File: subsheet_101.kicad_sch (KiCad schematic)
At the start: 6 parts, among them J03 Jumper wire, J04 Jumper wire

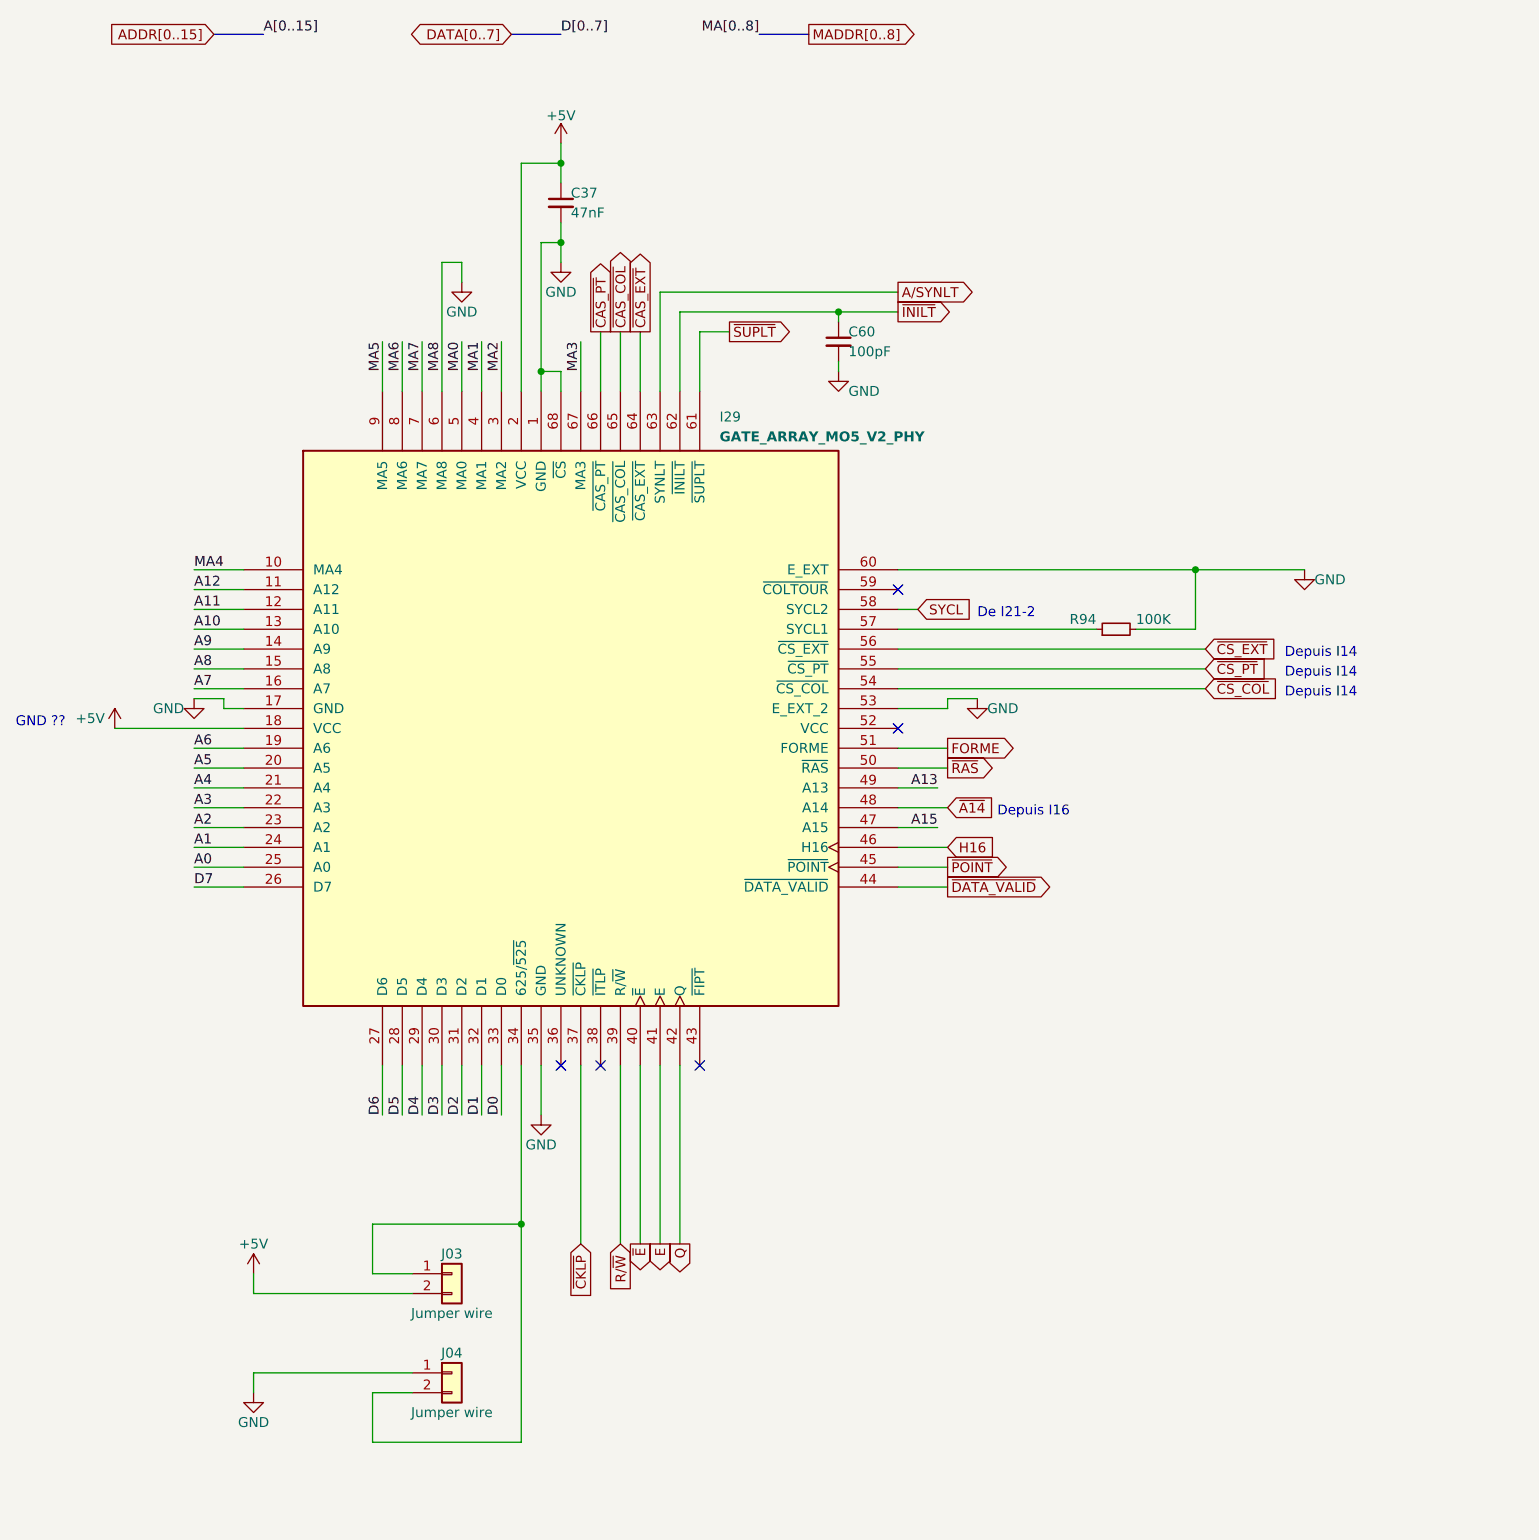
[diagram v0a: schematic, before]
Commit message: Various mentions, added C60bis to I29 on pin 62
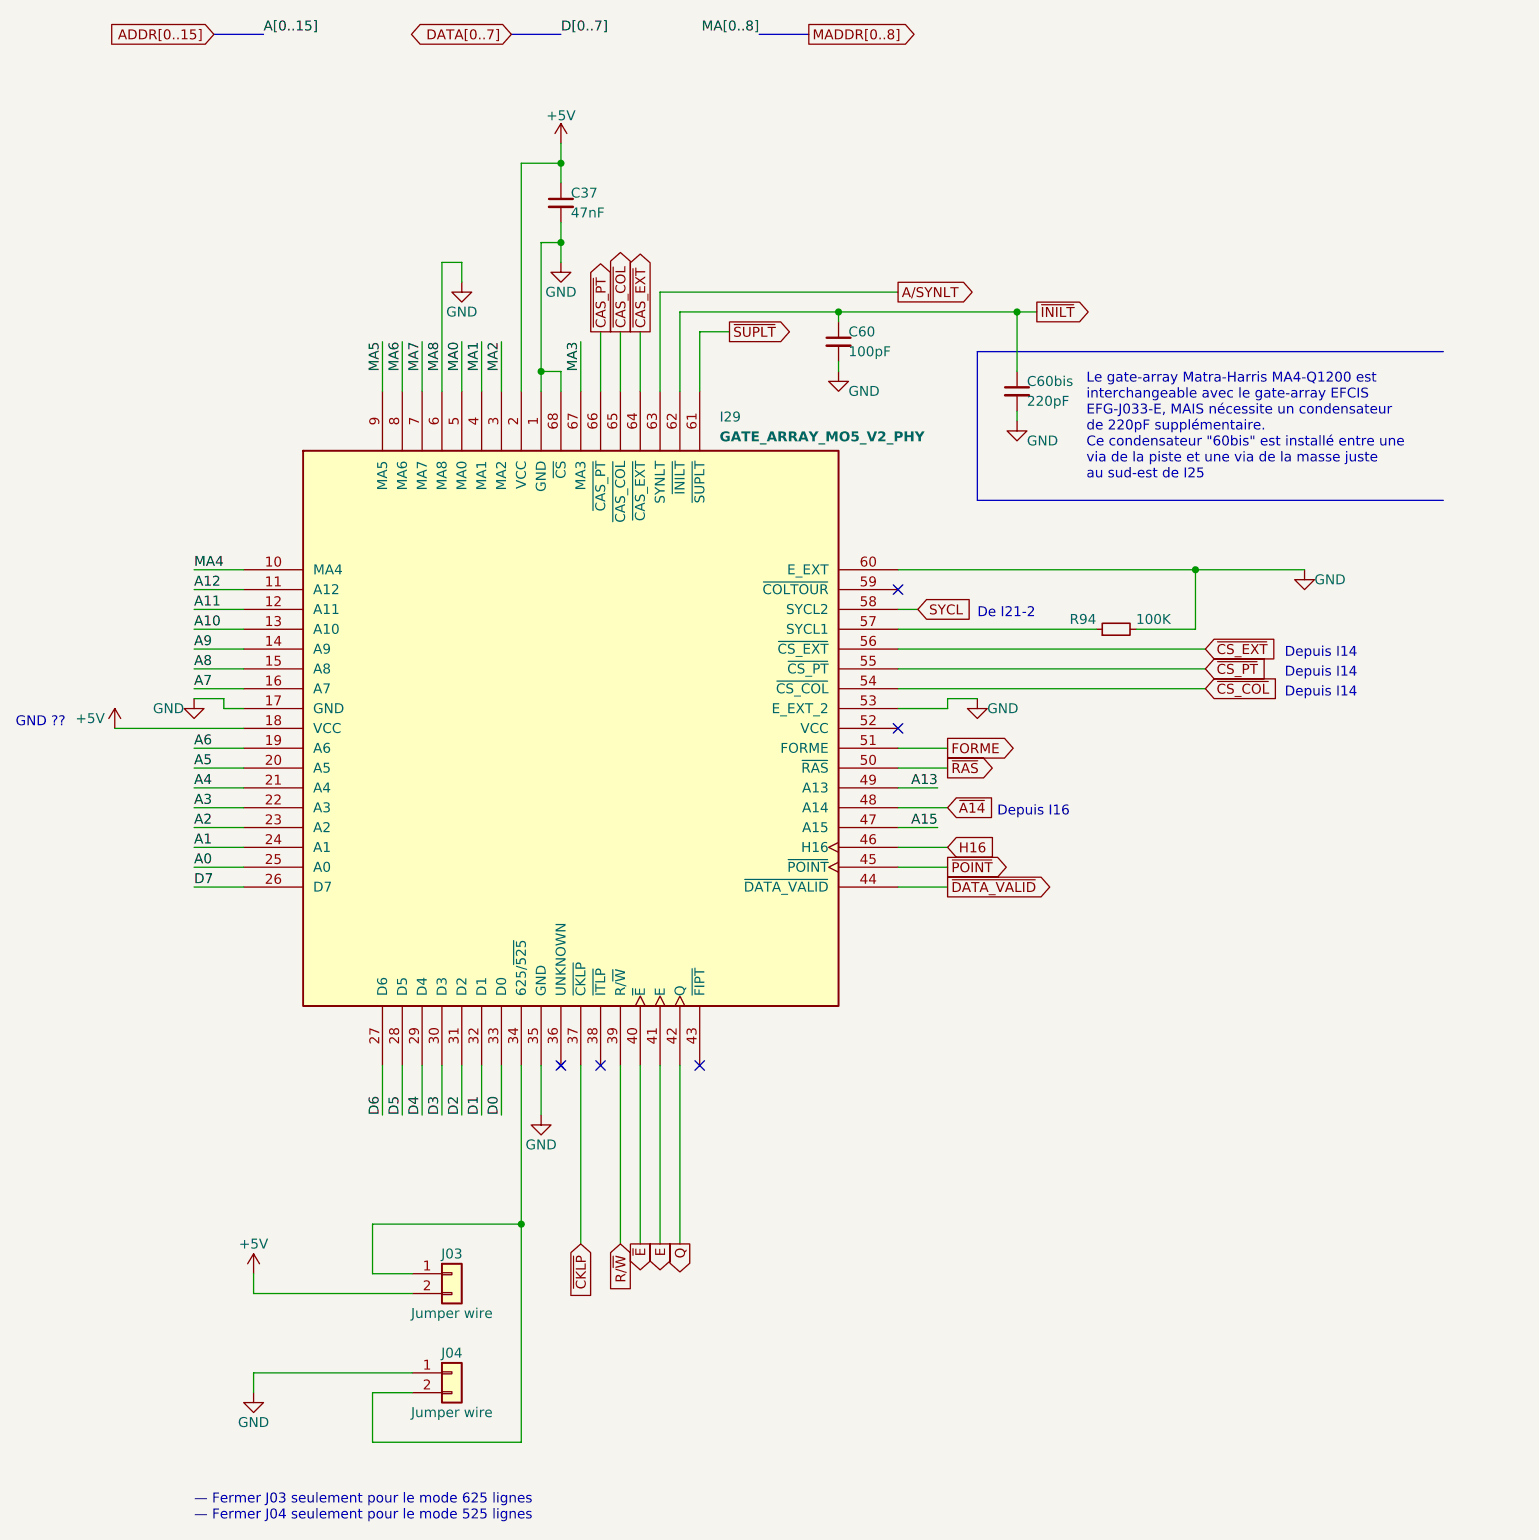
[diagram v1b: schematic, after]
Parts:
- added C60bis: 220pF, commons-passives_THT:Passive_THT_capacitor_mlcc_W2.54mm_L5.08mm, symbol Device:C_Small
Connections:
- net GND: now also C60bis.2
- net ~{INILT}: now also C60bis.1
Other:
- note added: "Le gate-array Matra-Harris MA4-Q1200 est interchangeable avec le gate-array EFCIS EFG-J033-E, MAIS nécessite un condensateur de 220pF supplémentaire. Ce condensateur "60bis" est installé entre une via de la piste et une via de la masse juste au sud-est de I25"
- note added: "— Fermer J03 seulement pour le mode 625 lignes — Fermer J04 seulement pour le mode 525 lignes"
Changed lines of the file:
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@@
   (junction (at 118.11 60.96) (diameter 0) (color 0 0 0 0)
+  )
+  (junction (at 140.97 60.96) (diameter 0) (color 0 0 0 0)
   )
   (junction (at 80.01 68.58) (diameter 0) (color 0 0 0 0)
@@
     (stroke (width 0) (type default))
   )
+  (wire (pts (xy 140.97 73.66) (xy 140.97 74.93))
+    (stroke (width 0) (type default))
+  )
   (wire (pts (xy 156.21 101.6) (xy 163.83 101.6))
     (stroke (width 0) (type default))
@@
     (stroke (width 0) (type default))
   )
-  (wire (pts (xy 125.73 60.96) (xy 118.11 60.96))
-    (stroke (width 0) (type default))
-  )
   (wire (pts (xy 59.69 64.77) (xy 59.69 71.12))
     (stroke (width 0) (type default))
@@
     (stroke (width 0) (type default))
   )
+  (polyline (pts (xy 135.89 85.09) (xy 195.58 85.09))
+    (stroke (width 0) (type default))
+  )
   (wire (pts (xy 118.11 67.31) (xy 118.11 68.58))
     (stroke (width 0) (type default))
@@
     (stroke (width 0) (type default))
   )
+  (wire (pts (xy 143.51 60.96) (xy 140.97 60.96))
+    (stroke (width 0) (type default))
+  )
   (wire (pts (xy 67.31 163.83) (xy 67.31 157.48))
     (stroke (width 0) (type default))
@@
     (stroke (width 0) (type default))
   )
+  (polyline (pts (xy 195.58 66.04) (xy 135.89 66.04))
+    (stroke (width 0) (type default))
+  )
   (wire (pts (xy 85.09 157.48) (xy 85.09 180.34))
     (stroke (width 0) (type default))
@@
     (stroke (width 0) (type default))
   )
+  (wire (pts (xy 140.97 60.96) (xy 140.97 68.58))
+    (stroke (width 0) (type default))
+  )
+  (polyline (pts (xy 135.89 66.04) (xy 135.89 85.09))
+    (stroke (width 0) (type default))
+  )
   (wire (pts (xy 77.47 41.91) (xy 82.55 41.91))
     (stroke (width 0) (type default))
@@
     (stroke (width 0) (type default))
   )
+  (wire (pts (xy 118.11 60.96) (xy 140.97 60.96))
+    (stroke (width 0) (type default))
+  )
   (wire (pts (xy 35.56 127) (xy 41.91 127))
     (stroke (width 0) (type default))
@@
     (effects (font (size 1.27 1.27)) (justify left bottom))
   )
+  (text "— Fermer J03 seulement pour le mode 625 lignes\n— Fermer J04 seulement pour le mode 525 lignes"
+    (at 35.56 215.9 0)
+    (effects (font (size 1.27 1.27)) (justify left bottom))
+  )
   (text "Depuis I14" (at 175.26 105.41 0)
+    (effects (font (size 1.27 1.27)) (justify left bottom))
+  )
+  (text "Le gate-array Matra-Harris MA4-Q1200 est\ninterchangeable avec le gate-array EFCIS\nEFG-J033-E, MAIS nécessite un condensateur\nde 220pF supplémentaire.\nCe condensateur \"60bis\" est installé entre une\nvia de la piste et une via de la masse juste\nau sud-est de I25"
+    (at 149.86 82.55 0)
     (effects (font (size 1.27 1.27)) (justify left bottom))
   )
@@
     )
   )
-  (global_label "~{INILT}" (shape output) (at 125.73 60.96 0) (fields_autoplaced)
-    (effects (font (size 1.27 1.27)) (justify left))
-    (property "Intersheetrefs" "${INTERSHEET_REFS}" (at 132.6788 60.8806 0)
+  (global_label "~{INILT}" (shape output) (at 143.51 60.96 0) (fields_autoplaced)
+    (effects (font (size 1.27 1.27)) (justify left))
+    (property "Intersheetrefs" "${INTERSHEET_REFS}" (at 150.4588 60.8806 0)
       (effects (font (size 1.27 1.27)) (justify left) hide)
     )
@@
     )
   )
+  (symbol (lib_id "power:GND") (at 140.97 74.93 0) (unit 1)
+    (in_bom yes) (on_board yes) (dnp no)
+    (property "Reference" "#PWR018" (at 140.97 81.28 0)
+      (effects (font (size 1.27 1.27)) hide)
+    )
+    (property "Value" "GND" (at 142.24 77.47 0)
+      (effects (font (size 1.27 1.27)) (justify left))
+    )
+    (property "Footprint" "" (at 140.97 74.93 0)
+      (effects (font (size 1.27 1.27)) hide)
+    )
+    (property "Datasheet" "" (at 140.97 74.93 0)
+      (effects (font (size 1.27 1.27)) hide)
+    )
+    (pin "1")
+    (instances
+      (project "UC-50-001"
+        (path "/e63e39d7-6ac0-4ffd-8aa3-1841a4541b55/f465a4b1-7c3c-40cc-9e66-ff9f17003d42"
+          (reference "#PWR018") (unit 1)
+        )
+      )
+    )
+  )
   (symbol (lib_id "power:GND") (at 69.85 57.15 0) (unit 1)
     (in_bom yes) (on_board yes) (dnp no)
@@
         )
       )
+    )
+  )
+  (symbol (lib_id "Device:C_Small") (at 140.97 71.12 0) (unit 1)
+    (in_bom yes) (on_board yes) (dnp no)
+    (property "Reference" "C60bis" (at 142.24 69.85 0)
+      (effects (font (size 1.27 1.27)) (justify left))
+    )
+    (property "Value" "220pF" (at 142.24 72.39 0)
+      (effects (font (size 1.27 1.27)) (justify left))
+    )
+    (property "Footprint" "commons-passives_THT:Passive_THT_capacitor_mlcc_W2.54mm_L5.08mm" (at 140.97 71.12 0)
+      (effects (font (size 1.27 1.27)) hide)
+    )
+    (property "Datasheet" "~" (at 140.97 71.12 0)
+      (effects (font (size 1.27 1.27)) hide)
+    )
+    (pin "1")
+    (pin "2")
+    (instances
+      (project "UC-50-001"
+        (path "/e63e39d7-6ac0-4ffd-8aa3-1841a4541b55/f465a4b1-7c3c-40cc-9e66-ff9f17003d42"
+          (reference "C60bis") (unit 1)
+        )
+      )

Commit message: mentions of the motherboards revisions
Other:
- note added: "Le gate-array Matra-Harris MA4-Q1200 est interchangeable avec le gate-array EFCIS EFG-J033-E, MAIS nécessite un condensateur de 220pF supplémentaire. Ce condensateur "60bis" est installé entre une via de la piste et une via de la masse juste au sud-est de I25. (POP 5007S, POP 5009S)"
- note removed: "Le gate-array Matra-Harris MA4-Q1200 est interchangeable avec le gate-array EFCIS EFG-J033-E, MAIS nécessite un condensateur de 220pF supplémentaire. Ce condensateur "60bis" est installé entre une via de la piste et une via de la masse juste au sud-est de I25"
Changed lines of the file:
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@@
     (rev "v2.0.0-alpha")
     (comment 1 "http://github.com/sporniket/kicad-conversions--thomson-mo5--v1")
-    (comment 3 "Gate Array EFCIS")
+    (comment 3 "Gate Array EFCIS EFG-J033-E / Matra-Harris MA4-Q1200 (POP 5007S, POP 5009S)")
+    (comment 4 "Références : POP 5003S, POP 5005S, POP 5007S, POP 5009S")
   )
   (junction (at 77.47 177.8) (diameter 0) (color 0 0 0 0)
@@
     (stroke (width 0) (type default))
   )
-  (polyline (pts (xy 135.89 85.09) (xy 195.58 85.09))
+  (polyline (pts (xy 135.89 87.63) (xy 195.58 87.63))
     (stroke (width 0) (type default))
   )
@@
     (stroke (width 0) (type default))
   )
-  (polyline (pts (xy 135.89 66.04) (xy 135.89 85.09))
+  (polyline (pts (xy 135.89 66.04) (xy 135.89 87.63))
     (stroke (width 0) (type default))
   )
@@
     (effects (font (size 1.27 1.27)) (justify left bottom))
   )
-  (text "Le gate-array Matra-Harris MA4-Q1200 est\ninterchangeable avec le gate-array EFCIS\nEFG-J033-E, MAIS nécessite un condensateur\nde 220pF supplémentaire.\nCe condensateur \"60bis\" est installé entre une\nvia de la piste et une via de la masse juste\nau sud-est de I25"
-    (at 149.86 82.55 0)
-    (effects (font (size 1.27 1.27)) (justify left bottom))
-  )
+  (text "Le gate-array Matra-Harris MA4-Q1200 est\ninterchangeable avec le gate-array EFCIS\nEFG-J033-E, MAIS nécessite un condensateur\nde 220pF supplémentaire.\nCe condensateur \"60bis\" est installé entre une\nvia de la piste et une via de la masse juste\nau sud-est de I25.\n\n(POP 5007S, POP 5009S)"
+    (at 149.86 85.09 0)
+    (effects (font (size 1.27 1.27)) (justify left bottom))
+  )

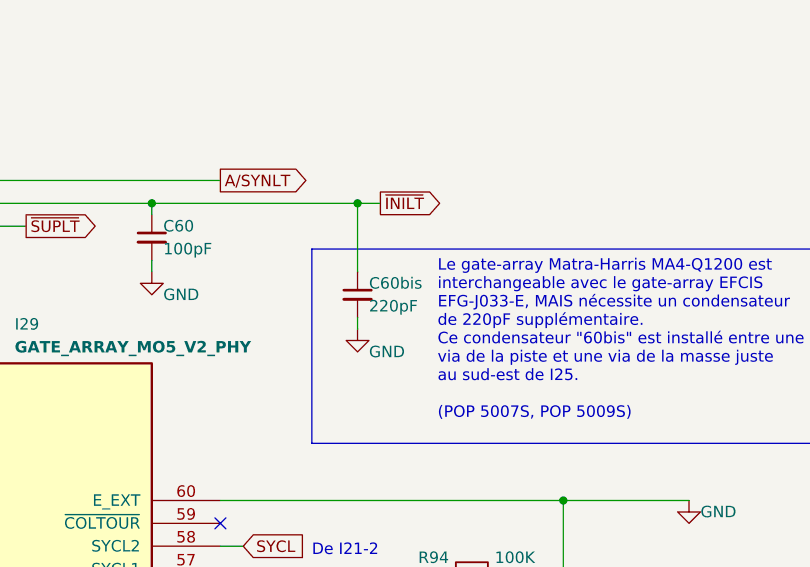
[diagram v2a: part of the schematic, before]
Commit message: fixed some naming, assigned footprints to symbols without one, added them to pcb
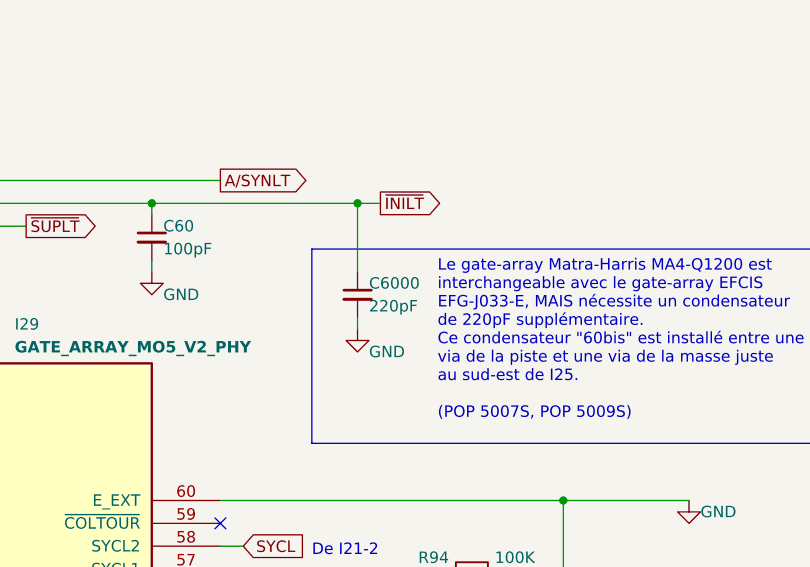
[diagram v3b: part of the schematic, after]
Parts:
- J03, J04: footprint (none) -> thomson-moto-passives:Passive_THT_jumper_wire_W2.54mm_L10.16mm
- renumbered C60bis to C6000
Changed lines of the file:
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@@
   (symbol (lib_id "Device:C_Small") (at 140.97 71.12 0) (unit 1)
     (in_bom yes) (on_board yes) (dnp no)
-    (property "Reference" "C60bis" (at 142.24 69.85 0)
+    (property "Reference" "C6000" (at 142.24 69.85 0)
       (effects (font (size 1.27 1.27)) (justify left))
     )
@@
       (project "UC-50-001"
         (path "/e63e39d7-6ac0-4ffd-8aa3-1841a4541b55/f465a4b1-7c3c-40cc-9e66-ff9f17003d42"
-          (reference "C60bis") (unit 1)
+          (reference "C6000") (unit 1)
         )
       )
@@
       (effects (font (size 1.27 1.27)))
     )
-    (property "Footprint" "" (at 68.58 184.15 0)
+    (property "Footprint" "thomson-moto-passives:Passive_THT_jumper_wire_W2.54mm_L10.16mm" (at 68.58 184.15 0)
       (effects (font (size 1.27 1.27)) hide)
     )
@@
       (effects (font (size 1.27 1.27)))
     )
-    (property "Footprint" "" (at 68.58 196.85 0)
-      (effects (font (size 1.27 1.27)) hide)
-    )
+    (property "Footprint" "thomson-moto-passives:Passive_THT_jumper_wire_W2.54mm_L10.16mm" (at 68.58 196.85 0)
+      (effects (font (size 1.27 1.27)) hide)
+    )
